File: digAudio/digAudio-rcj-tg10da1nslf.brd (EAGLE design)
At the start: 19.4 x 31 mm, 16 parts, among them IC1 DIT4096-H

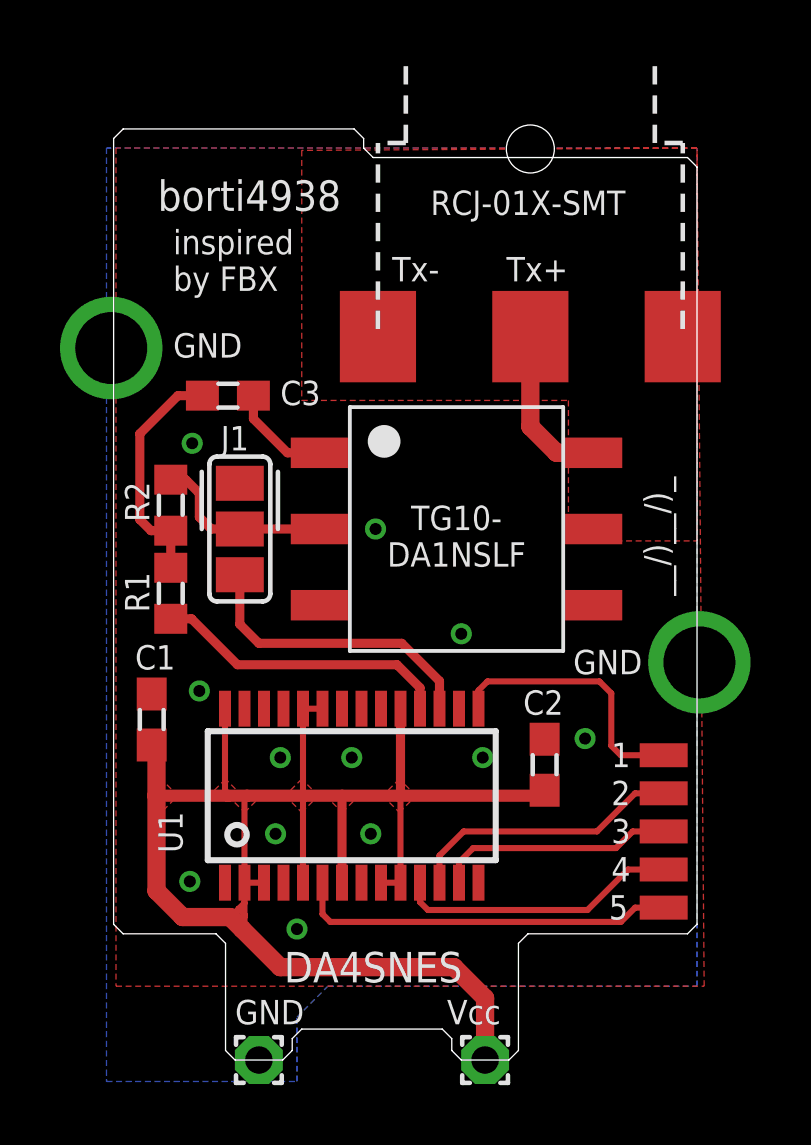
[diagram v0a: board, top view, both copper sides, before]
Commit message: bugfix on PCBs: - pin 14 (M/nS) was floating - now it is properly connected to GND
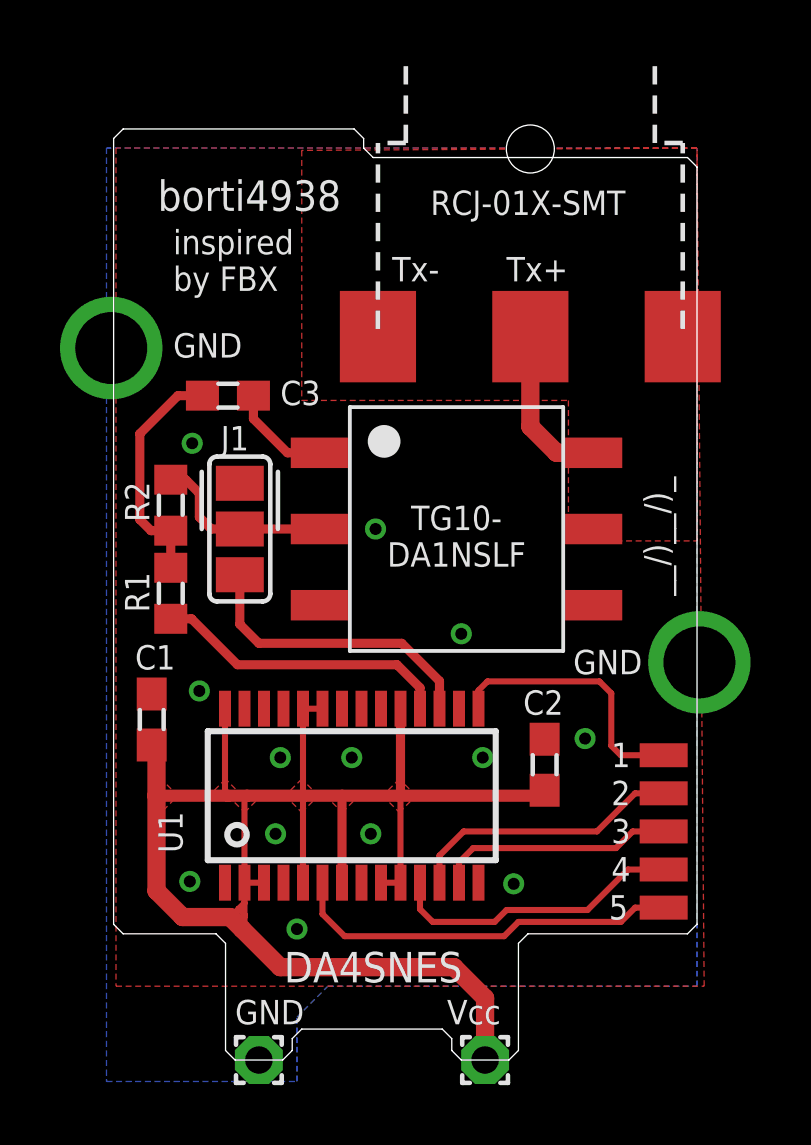
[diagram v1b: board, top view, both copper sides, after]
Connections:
- net GND: now also IC1.14
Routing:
- net GND: vias 14 -> 15
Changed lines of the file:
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@@
 <?xml version="1.0" encoding="utf-8"?>
 <!DOCTYPE eagle SYSTEM "eagle.dtd">
-<eagle version="8.5.2">
+<eagle version="9.6.2">
 <drawing>
 <settings>
@@
 <param name="checkStop" value="0"/>
 <param name="checkValues" value="0"/>
+<param name="checkNames" value="1"/>
+<param name="checkWireStubs" value="1"/>
+<param name="checkPolygonWidth" value="0"/>
 <param name="useDiameter" value="13"/>
 <param name="maxErrors" value="50"/>
@@
 <vertex x="-7.62" y="21.59"/>
 </polygon>
+<contactref element="IC1" pad="14"/>
+<via x="5.953125" y="-2.936875" extent="1-16" drill="0.4"/>
 </signal>
 <signal name="VCC">
@@
 <contactref element="IC1" pad="6"/>
 <contactref element="5" pad="P$1"/>
-<wire x1="-0.419375" y1="-2.9" x2="-0.419375" y2="-3.94625" width="0.2032" layer="1"/>
-<wire x1="-0.419375" y1="-3.94625" x2="-0.15875" y2="-4.206875" width="0.2032" layer="1"/>
-<wire x1="-0.15875" y1="-4.206875" x2="9.525" y2="-4.206875" width="0.2032" layer="1"/>
+<wire x1="-0.419375" y1="-3.94625" x2="-0.419375" y2="-2.9" width="0.2032" layer="1"/>
+<wire x1="9.525" y1="-4.206875" x2="6.111875" y2="-4.206875" width="0.2032" layer="1"/>
 <wire x1="9.525" y1="-4.206875" x2="10.00125" y2="-3.730625" width="0.2032" layer="1"/>
 <wire x1="10.00125" y1="-3.730625" x2="10.95375" y2="-3.730625" width="0.2032" layer="1"/>
+<wire x1="6.111875" y1="-4.206875" x2="5.635625" y2="-4.683125" width="0.2032" layer="1"/>
+<wire x1="5.635625" y1="-4.683125" x2="0.3175" y2="-4.683125" width="0.2032" layer="1"/>
+<wire x1="0.3175" y1="-4.683125" x2="-0.419375" y2="-3.94625" width="0.2032" layer="1"/>
 </signal>
 <signal name="N$4">
@@
 <wire x1="10.95375" y1="-2.460625" x2="9.763125" y2="-2.460625" width="0.2032" layer="1"/>
 <wire x1="9.763125" y1="-2.460625" x2="8.41375" y2="-3.81" width="0.2032" layer="1"/>
-<wire x1="8.41375" y1="-3.81" x2="3.095625" y2="-3.81" width="0.2032" layer="1"/>
-<wire x1="2.830625" y1="-3.545" x2="2.830625" y2="-2.9" width="0.2032" layer="1"/>
-<wire x1="3.095625" y1="-3.81" x2="2.830625" y2="-3.545" width="0.2032" layer="1"/>
+<wire x1="8.41375" y1="-3.81" x2="5.715" y2="-3.81" width="0.2032" layer="1"/>
+<wire x1="2.830625" y1="-3.783125" x2="2.830625" y2="-2.9" width="0.2032" layer="1"/>
+<wire x1="5.715" y1="-3.81" x2="5.318125" y2="-4.206875" width="0.2032" layer="1"/>
+<wire x1="5.318125" y1="-4.206875" x2="3.254375" y2="-4.206875" width="0.2032" layer="1"/>
+<wire x1="3.254375" y1="-4.206875" x2="2.830625" y2="-3.783125" width="0.2032" layer="1"/>
 </signal>
 <signal name="N$5">
@@
 </signal>
 </signals>
+<mfgpreviewcolors>
+<mfgpreviewcolor name="soldermaskcolor" color="0xC8008000"/>
+<mfgpreviewcolor name="silkscreencolor" color="0xFFFEFEFE"/>
+<mfgpreviewcolor name="backgroundcolor" color="0xFF282828"/>
+<mfgpreviewcolor name="coppercolor" color="0xFFFFBF00"/>
+<mfgpreviewcolor name="substratecolor" color="0xFF786E46"/>
+</mfgpreviewcolors>
 <errors>
 </errors>
